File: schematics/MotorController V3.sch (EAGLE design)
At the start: 54 parts, among them IC1 7805, Q1 BC307

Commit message: no message
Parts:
- renumbered U$3 to U$2
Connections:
- net +5V: now also IMU-I2C.4, U$2.D0; no longer U$2.VIN
- net 3.3V: now also IMU-I2C.5; no longer IMU-I2C.4
- net D0: now also U$2.VIN; no longer U$2.D0
- net GND: now also U$2.3V@2, U$2.D1, U$2.SK; no longer IMU-I2C.5, U$2.GND@1, U$2.GND@2, U$2.GND@4
- net RST: now also U$2.D2; no longer U$2.RST
- net SCL1: now also U$2.RST; no longer U$2.D2
- net SDA1: now also U$2.GND@2; no longer U$2.D1
- net TX5: now also U$2.S3; no longer U$2.RX
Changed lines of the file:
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@@
 <part name="D12" library="diode" library_urn="urn:adsk.eagle:library:210" deviceset="ZENER-DIODE" device="DO41Z10" package3d_urn="urn:adsk.eagle:package:43341/1" value="5.6V"/>
 <part name="D13" library="diode" library_urn="urn:adsk.eagle:library:210" deviceset="ZENER-DIODE" device="DO41Z10" package3d_urn="urn:adsk.eagle:package:43341/1" value="5.6V"/>
-<part name="U$3" library="nodemcu" deviceset="NODEMCU" device="NODEMCUV2" value="NODEMCUNODEMCUV2"/>
 <part name="LED1" library="led" library_urn="urn:adsk.eagle:library:259" deviceset="LED" device="3MM" package3d_urn="urn:adsk.eagle:package:15797/1" value="red"/>
 <part name="R15" library="rcl" library_urn="urn:adsk.eagle:library:334" deviceset="R-EU_" device="0207/10" package3d_urn="urn:adsk.eagle:package:23491/1" value="4,7K"/>
@@
 <part name="MOTOR3" library="con-molex" deviceset="5566-4" device=""/>
 <part name="D14" library="diode" library_urn="urn:adsk.eagle:library:210" deviceset="ZENER-DIODE" device="DO41Z10" package3d_urn="urn:adsk.eagle:package:43341/1" value="5.6V"/>
+<part name="U$2" library="nodemcu" deviceset="NODEMCU" device="NODEMCUV2"/>
 </parts>
 <sheets>
@@
 <attribute name="VALUE" x="135.509" y="-17.018" size="1.778" layer="96" rot="R90"/>
 </instance>
-<instance part="U$3" gate="G$1" x="93.98" y="205.74" rot="R180"/>
 <instance part="LED1" gate="G$1" x="-27.94" y="-15.24" rot="R180">
 <attribute name="NAME" x="-34.036" y="-13.208" size="1.778" layer="95" rot="R270"/>
@@
 <attribute name="NAME" x="-29.845" y="16.002" size="1.778" layer="95" rot="R90"/>
 <attribute name="VALUE" x="-24.511" y="16.002" size="1.778" layer="96" rot="R90"/>
+</instance>
+<instance part="U$2" gate="G$1" x="93.98" y="205.74">
+<attribute name="NAME" x="93.98" y="213.36" size="1.778" layer="94"/>
+<attribute name="VALUE" x="81.28" y="228.6" size="1.778" layer="94"/>
 </instance>
 </instances>
@@
 <wire x1="177.8" y1="50.8" x2="177.8" y2="73.66" width="0.1524" layer="91"/>
 <wire x1="177.8" y1="73.66" x2="177.8" y2="91.44" width="0.1524" layer="91"/>
-<wire x1="27.94" y1="149.86" x2="121.92" y2="149.86" width="0.1524" layer="91"/>
+<wire x1="27.94" y1="149.86" x2="50.8" y2="149.86" width="0.1524" layer="91"/>
+<wire x1="50.8" y1="149.86" x2="121.92" y2="149.86" width="0.1524" layer="91"/>
 <wire x1="121.92" y1="149.86" x2="154.94" y2="149.86" width="0.1524" layer="91"/>
 <wire x1="154.94" y1="149.86" x2="177.8" y2="149.86" width="0.1524" layer="91"/>
@@
 <wire x1="-91.44" y1="50.8" x2="-91.44" y2="45.72" width="0.1524" layer="91"/>
 <junction x="154.94" y="149.86"/>
-<pinref part="U$3" gate="G$1" pin="VIN"/>
 <wire x1="154.94" y1="167.64" x2="154.94" y2="149.86" width="0.1524" layer="91"/>
 <wire x1="114.3" y1="223.52" x2="121.92" y2="223.52" width="0.1524" layer="91"/>
@@
 <label x="177.8" y="91.44" size="1.778" layer="95"/>
 <label x="236.22" y="132.08" size="1.778" layer="95"/>
+<pinref part="IMU-I2C" gate="G$1" pin="4"/>
+<wire x1="50.8" y1="170.18" x2="50.8" y2="149.86" width="0.1524" layer="91"/>
+<junction x="50.8" y="149.86"/>
+<pinref part="U$2" gate="G$1" pin="D0"/>
 </segment>
 </net>
@@
 <wire x1="175.26" y1="86.36" x2="182.88" y2="86.36" width="0.1524" layer="91"/>
 <wire x1="190.5" y1="38.1" x2="190.5" y2="-22.86" width="0.1524" layer="91"/>
-<wire x1="53.34" y1="124.46" x2="17.78" y2="124.46" width="0.1524" layer="91"/>
+<wire x1="60.96" y1="124.46" x2="17.78" y2="124.46" width="0.1524" layer="91"/>
 <wire x1="17.78" y1="124.46" x2="15.24" y2="124.46" width="0.1524" layer="91"/>
 <wire x1="15.24" y1="124.46" x2="-12.7" y2="124.46" width="0.1524" layer="91"/>
@@
 <wire x1="-109.22" y1="38.1" x2="-109.22" y2="-22.86" width="0.1524" layer="91"/>
 <junction x="-109.22" y="-22.86"/>
-<pinref part="IMU-I2C" gate="G$1" pin="5"/>
 <wire x1="-55.88" y1="-17.78" x2="-55.88" y2="-22.86" width="0.1524" layer="91"/>
 <junction x="-55.88" y="-22.86"/>
@@
 <wire x1="137.16" y1="124.46" x2="116.84" y2="124.46" width="0.1524" layer="91"/>
 <wire x1="116.84" y1="124.46" x2="60.96" y2="124.46" width="0.1524" layer="91"/>
-<wire x1="60.96" y1="124.46" x2="53.34" y2="124.46" width="0.1524" layer="91"/>
 <wire x1="15.24" y1="129.54" x2="15.24" y2="124.46" width="0.1524" layer="91"/>
 <junction x="15.24" y="124.46"/>
@@
 <wire x1="132.08" y1="-17.78" x2="132.08" y2="-22.86" width="0.1524" layer="91"/>
 <junction x="132.08" y="-22.86"/>
-<wire x1="53.34" y1="170.18" x2="53.34" y2="124.46" width="0.1524" layer="91"/>
-<junction x="53.34" y="124.46"/>
 <wire x1="63.5" y1="-10.16" x2="63.5" y2="-22.86" width="0.1524" layer="91"/>
 <junction x="63.5" y="-22.86"/>
@@
 <junction x="175.26" y="45.72"/>
 <wire x1="175.26" y1="38.1" x2="190.5" y2="38.1" width="0.1524" layer="91"/>
-<pinref part="U$3" gate="G$1" pin="GND@4"/>
 <wire x1="73.66" y1="203.2" x2="60.96" y2="203.2" width="0.1524" layer="91"/>
 <wire x1="60.96" y1="203.2" x2="60.96" y2="124.46" width="0.1524" layer="91"/>
 <junction x="60.96" y="124.46"/>
-<pinref part="U$3" gate="G$1" pin="GND@2"/>
 <wire x1="114.3" y1="220.98" x2="116.84" y2="220.98" width="0.1524" layer="91"/>
-<pinref part="U$3" gate="G$1" pin="GND@3"/>
 <wire x1="73.66" y1="220.98" x2="60.96" y2="220.98" width="0.1524" layer="91"/>
 <wire x1="60.96" y1="220.98" x2="60.96" y2="203.2" width="0.1524" layer="91"/>
@@
 <junction x="137.16" y="124.46"/>
 <label x="134.62" y="162.56" size="1.778" layer="95"/>
-<pinref part="U$3" gate="G$1" pin="GND"/>
 <wire x1="114.3" y1="190.5" x2="116.84" y2="190.5" width="0.1524" layer="91"/>
 <wire x1="116.84" y1="190.5" x2="116.84" y2="210.82" width="0.1524" layer="91"/>
-<pinref part="U$3" gate="G$1" pin="GND@1"/>
 <wire x1="116.84" y1="210.82" x2="114.3" y2="210.82" width="0.1524" layer="91"/>
 <wire x1="116.84" y1="210.82" x2="116.84" y2="220.98" width="0.1524" layer="91"/>
@@
 <wire x1="-27.94" y1="-17.78" x2="-27.94" y2="-22.86" width="0.1524" layer="91"/>
 <junction x="-27.94" y="-22.86"/>
+<pinref part="U$2" gate="G$1" pin="GND"/>
+<pinref part="U$2" gate="G$1" pin="SK"/>
+<pinref part="U$2" gate="G$1" pin="GND@3"/>
+<pinref part="U$2" gate="G$1" pin="3V@2"/>
+<pinref part="U$2" gate="G$1" pin="D1"/>
 </segment>
 </net>
@@
 <wire x1="73.66" y1="154.94" x2="73.66" y2="114.3" width="0.1524" layer="91"/>
 <label x="73.66" y="114.3" size="1.778" layer="95" rot="R90"/>
-<pinref part="U$3" gate="G$1" pin="D2"/>
 <wire x1="68.58" y1="193.04" x2="73.66" y2="193.04" width="0.1524" layer="91"/>
 <wire x1="68.58" y1="193.04" x2="68.58" y2="154.94" width="0.1524" layer="91"/>
 <wire x1="68.58" y1="154.94" x2="73.66" y2="154.94" width="0.1524" layer="91"/>
+<pinref part="U$2" gate="G$1" pin="RST"/>
 </segment>
 </net>
@@
 <pinref part="PRJ1" gate="G$1" pin="37/A18"/>
 <label x="76.2" y="114.3" size="1.778" layer="95" rot="R90"/>
-<pinref part="U$3" gate="G$1" pin="D1"/>
 <wire x1="76.2" y1="157.48" x2="76.2" y2="114.3" width="0.1524" layer="91"/>
 <wire x1="73.66" y1="190.5" x2="71.12" y2="190.5" width="0.1524" layer="91"/>
 <wire x1="71.12" y1="190.5" x2="71.12" y2="157.48" width="0.1524" layer="91"/>
 <wire x1="71.12" y1="157.48" x2="76.2" y2="157.48" width="0.1524" layer="91"/>
+<pinref part="U$2" gate="G$1" pin="GND@2"/>
 </segment>
 </net>
@@
 <pinref part="PRJ1" gate="G$1" pin="3V3_LO"/>
 <wire x1="33.02" y1="114.3" x2="33.02" y2="132.08" width="0.1524" layer="91"/>
-<wire x1="33.02" y1="132.08" x2="50.8" y2="132.08" width="0.1524" layer="91"/>
-<pinref part="IMU-I2C" gate="G$1" pin="4"/>
-<wire x1="50.8" y1="132.08" x2="50.8" y2="152.4" width="0.1524" layer="91"/>
-<wire x1="50.8" y1="152.4" x2="50.8" y2="170.18" width="0.1524" layer="91"/>
+<wire x1="33.02" y1="132.08" x2="53.34" y2="132.08" width="0.1524" layer="91"/>
+<wire x1="53.34" y1="132.08" x2="53.34" y2="152.4" width="0.1524" layer="91"/>
 <label x="33.02" y="132.08" size="1.778" layer="95"/>
 <wire x1="152.4" y1="165.1" x2="152.4" y2="152.4" width="0.1524" layer="91"/>
-<wire x1="152.4" y1="152.4" x2="50.8" y2="152.4" width="0.1524" layer="91"/>
-<junction x="50.8" y="152.4"/>
+<wire x1="152.4" y1="152.4" x2="53.34" y2="152.4" width="0.1524" layer="91"/>
 <label x="134.62" y="165.1" size="1.778" layer="95"/>
 <pinref part="CONTROL" gate="1" pin="2"/>
 <wire x1="134.62" y1="165.1" x2="152.4" y2="165.1" width="0.1524" layer="91"/>
+<pinref part="IMU-I2C" gate="G$1" pin="5"/>
+<wire x1="53.34" y1="170.18" x2="53.34" y2="152.4" width="0.1524" layer="91"/>
+<junction x="53.34" y="152.4"/>
 </segment>
 </net>
@@
 <wire x1="86.36" y1="157.48" x2="86.36" y2="180.34" width="0.1524" layer="91"/>
 <wire x1="86.36" y1="180.34" x2="63.5" y2="180.34" width="0.1524" layer="91"/>
-<pinref part="U$3" gate="G$1" pin="RX"/>
 <wire x1="73.66" y1="215.9" x2="63.5" y2="215.9" width="0.1524" layer="91"/>
 <wire x1="63.5" y1="180.34" x2="63.5" y2="215.9" width="0.1524" layer="91"/>
@@
 <junction x="86.36" y="157.48"/>
 <label x="134.62" y="170.18" size="1.778" layer="95"/>
+<pinref part="U$2" gate="G$1" pin="S3"/>
 </segment>
 </net>
@@
 <pinref part="CONTROL" gate="1" pin="7"/>
 <wire x1="144.78" y1="177.8" x2="134.62" y2="177.8" width="0.1524" layer="91"/>
-<pinref part="U$3" gate="G$1" pin="RST"/>
 <wire x1="114.3" y1="218.44" x2="144.78" y2="218.44" width="0.1524" layer="91"/>
 <label x="134.62" y="177.8" size="1.778" layer="95"/>
+<pinref part="U$2" gate="G$1" pin="D2"/>
 </segment>
 </net>
@@
 <net name="D0" class="0">
 <segment>
-<pinref part="U$3" gate="G$1" pin="D0"/>
 <wire x1="73.66" y1="187.96" x2="73.66" y2="182.88" width="0.1524" layer="91"/>
 <wire x1="73.66" y1="182.88" x2="139.7" y2="182.88" width="0.1524" layer="91"/>
@@
 <wire x1="139.7" y1="180.34" x2="134.62" y2="180.34" width="0.1524" layer="91"/>
 <label x="134.62" y="180.34" size="1.778" layer="95"/>
-</segment>
-</net>
+<pinref part="U$2" gate="G$1" pin="VIN"/>
+</segment>
+</net>

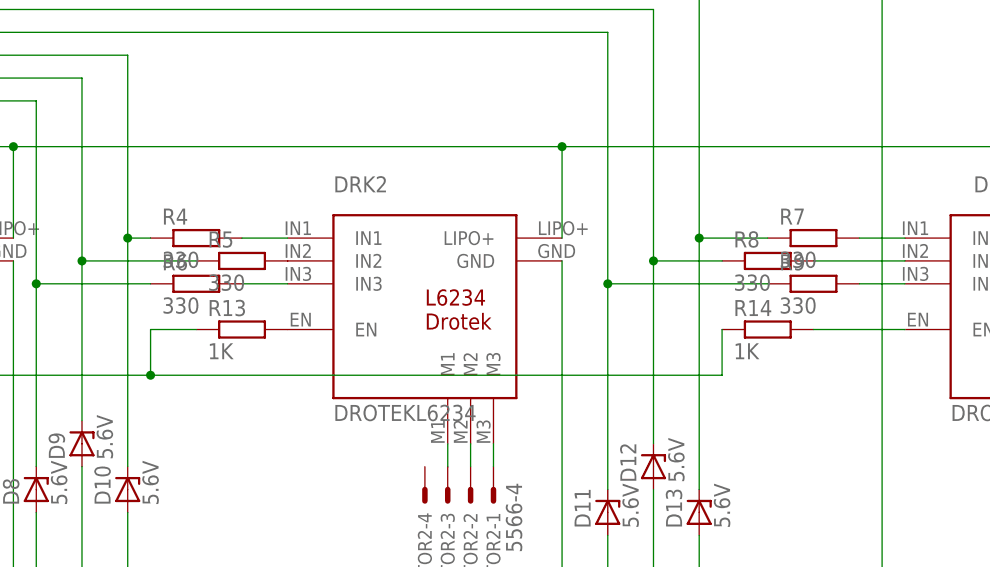
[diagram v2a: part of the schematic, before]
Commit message: more aggressive Motor PID
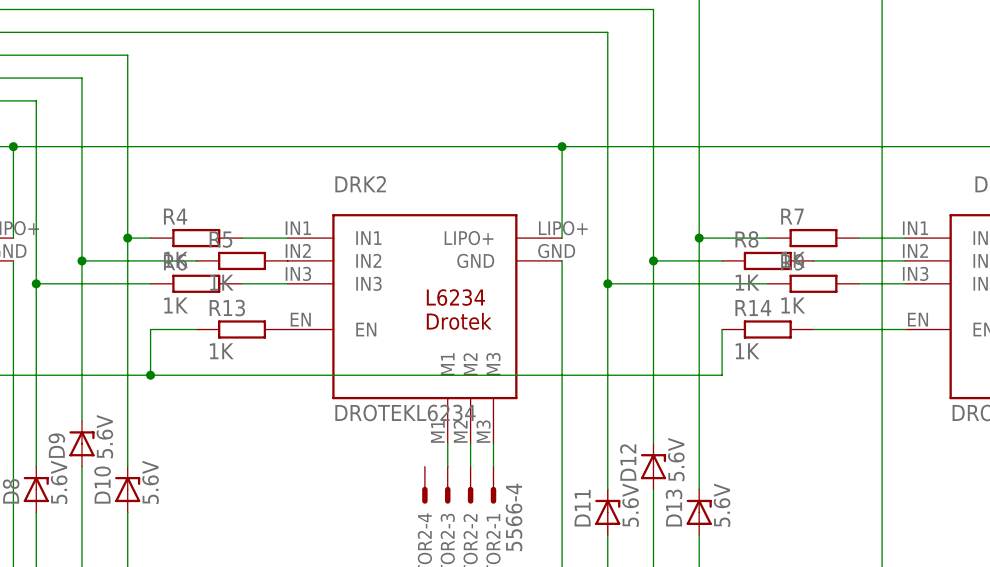
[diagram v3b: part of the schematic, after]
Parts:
- R4, R5, R6, R7, R8, R9: value 330 -> 1K
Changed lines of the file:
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@@
 <classes>
 <class number="0" name="default" width="0.254" drill="0.635">
-<clearance class="0" value="0.635"/>
+<clearance class="0" value="0.508"/>
 </class>
 <class number="1" name="Powerline" width="1" drill="0.635">
-<clearance class="1" value="0.635"/>
+<clearance class="1" value="0.508"/>
 </class>
 </classes>
@@
 <part name="DRK2" library="Drotek L6234" deviceset="DROTEKL6234" device=""/>
 <part name="DRK3" library="Drotek L6234" deviceset="DROTEKL6234" device=""/>
-<part name="R4" library="rcl" library_urn="urn:adsk.eagle:library:334" deviceset="R-EU_" device="0207/10" package3d_urn="urn:adsk.eagle:package:23491/1" value="330"/>
-<part name="R5" library="rcl" library_urn="urn:adsk.eagle:library:334" deviceset="R-EU_" device="0207/10" package3d_urn="urn:adsk.eagle:package:23491/1" value="330"/>
-<part name="R6" library="rcl" library_urn="urn:adsk.eagle:library:334" deviceset="R-EU_" device="0207/10" package3d_urn="urn:adsk.eagle:package:23491/1" value="330"/>
-<part name="R7" library="rcl" library_urn="urn:adsk.eagle:library:334" deviceset="R-EU_" device="0207/10" package3d_urn="urn:adsk.eagle:package:23491/1" value="330"/>
-<part name="R8" library="rcl" library_urn="urn:adsk.eagle:library:334" deviceset="R-EU_" device="0207/10" package3d_urn="urn:adsk.eagle:package:23491/1" value="330"/>
-<part name="R9" library="rcl" library_urn="urn:adsk.eagle:library:334" deviceset="R-EU_" device="0207/10" package3d_urn="urn:adsk.eagle:package:23491/1" value="330"/>
+<part name="R4" library="rcl" library_urn="urn:adsk.eagle:library:334" deviceset="R-EU_" device="0207/10" package3d_urn="urn:adsk.eagle:package:23491/1" value="1K"/>
+<part name="R5" library="rcl" library_urn="urn:adsk.eagle:library:334" deviceset="R-EU_" device="0207/10" package3d_urn="urn:adsk.eagle:package:23491/1" value="1K"/>
+<part name="R6" library="rcl" library_urn="urn:adsk.eagle:library:334" deviceset="R-EU_" device="0207/10" package3d_urn="urn:adsk.eagle:package:23491/1" value="1K"/>
+<part name="R7" library="rcl" library_urn="urn:adsk.eagle:library:334" deviceset="R-EU_" device="0207/10" package3d_urn="urn:adsk.eagle:package:23491/1" value="1K"/>
+<part name="R8" library="rcl" library_urn="urn:adsk.eagle:library:334" deviceset="R-EU_" device="0207/10" package3d_urn="urn:adsk.eagle:package:23491/1" value="1K"/>
+<part name="R9" library="rcl" library_urn="urn:adsk.eagle:library:334" deviceset="R-EU_" device="0207/10" package3d_urn="urn:adsk.eagle:package:23491/1" value="1K"/>
 <part name="R10" library="rcl" library_urn="urn:adsk.eagle:library:334" deviceset="R-EU_" device="0207/10" package3d_urn="urn:adsk.eagle:package:23491/1" value="1K"/>
 <part name="ENCODER3" library="con-lstb" library_urn="urn:adsk.eagle:library:162" deviceset="MA04-1" device="" package3d_urn="urn:adsk.eagle:package:8337/1" value="1"/>

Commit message: no message
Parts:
- removed ENCODER1, ENCODER2, ENCODER3: 1, con-lstb:MA04-1
- added ENC0, ENC1, ENC2: (no value), con-lstb:MA06-1
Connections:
- removed net +5V: C1.+, C3.1, CONTROL.3, D3.A, DC-MOTOR.4, ENCODER1.2, ENCODER2.2, ENCODER3.2, IC1.OUT, IMU-I2C.4, PRJ1.VIN, Q1.E, U$1.VDD(+5V), U$2.D0
- removed net ENC1_A: ENCODER1.3, PRJ1.11/MOSI
- removed net ENC1_B: ENCODER1.1, PRJ1.12/MISO
- removed net ENC2_A: ENCODER2.3, PRJ1.25
- removed net ENC2_B: ENCODER2.1, PRJ1.26
- removed net ENC3_A: ENCODER3.3, PRJ1.27
- removed net ENC3_B: ENCODER3.1, PRJ1.28
- new net +3.6V: C1.+, C3.1, CONTROL.3, D3.A, DC-MOTOR.4, IC1.OUT, IMU-I2C.4, PRJ1.VIN, Q1.E, U$1.VDD(+5V), U$2.D0
- new net CS0: ENC0.2, PRJ1.26
- new net CS1: ENC1.2, PRJ1.25
- new net CS2: ENC2.2, PRJ1.28
- new net MISO: ENC0.5, ENC1.5, ENC2.5, PRJ1.12/MISO
- new net MOSI: ENC0.4, ENC1.4, ENC2.4, PRJ1.11/MOSI
- new net SCK: ENC0.3, ENC1.3, ENC2.3, PRJ1.27
- net 3.3V: now also ENC0.1, ENC1.1, ENC2.1
- net GND: now also ENC0.6, ENC1.6, ENC2.6; no longer ENCODER1.4, ENCODER2.4, ENCODER3.4
